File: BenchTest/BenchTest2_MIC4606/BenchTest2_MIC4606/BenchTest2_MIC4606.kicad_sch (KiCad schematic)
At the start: 46 parts, among them J1 Conn_01x01_Socket, J2 Conn_01x01_Socket, J3 Conn_01x01_Socket, J4 Conn_01x01_Socket, J5 Conn_01x01_Socket, J6 Conn_01x01_Socket, J9 Conn_01x02_Socket, Q1 Q_NMOS_GDS, Q2 Q_NMOS_GDS, Q3 Q_NMOS_GDS, Q4 Q_NMOS_GDS

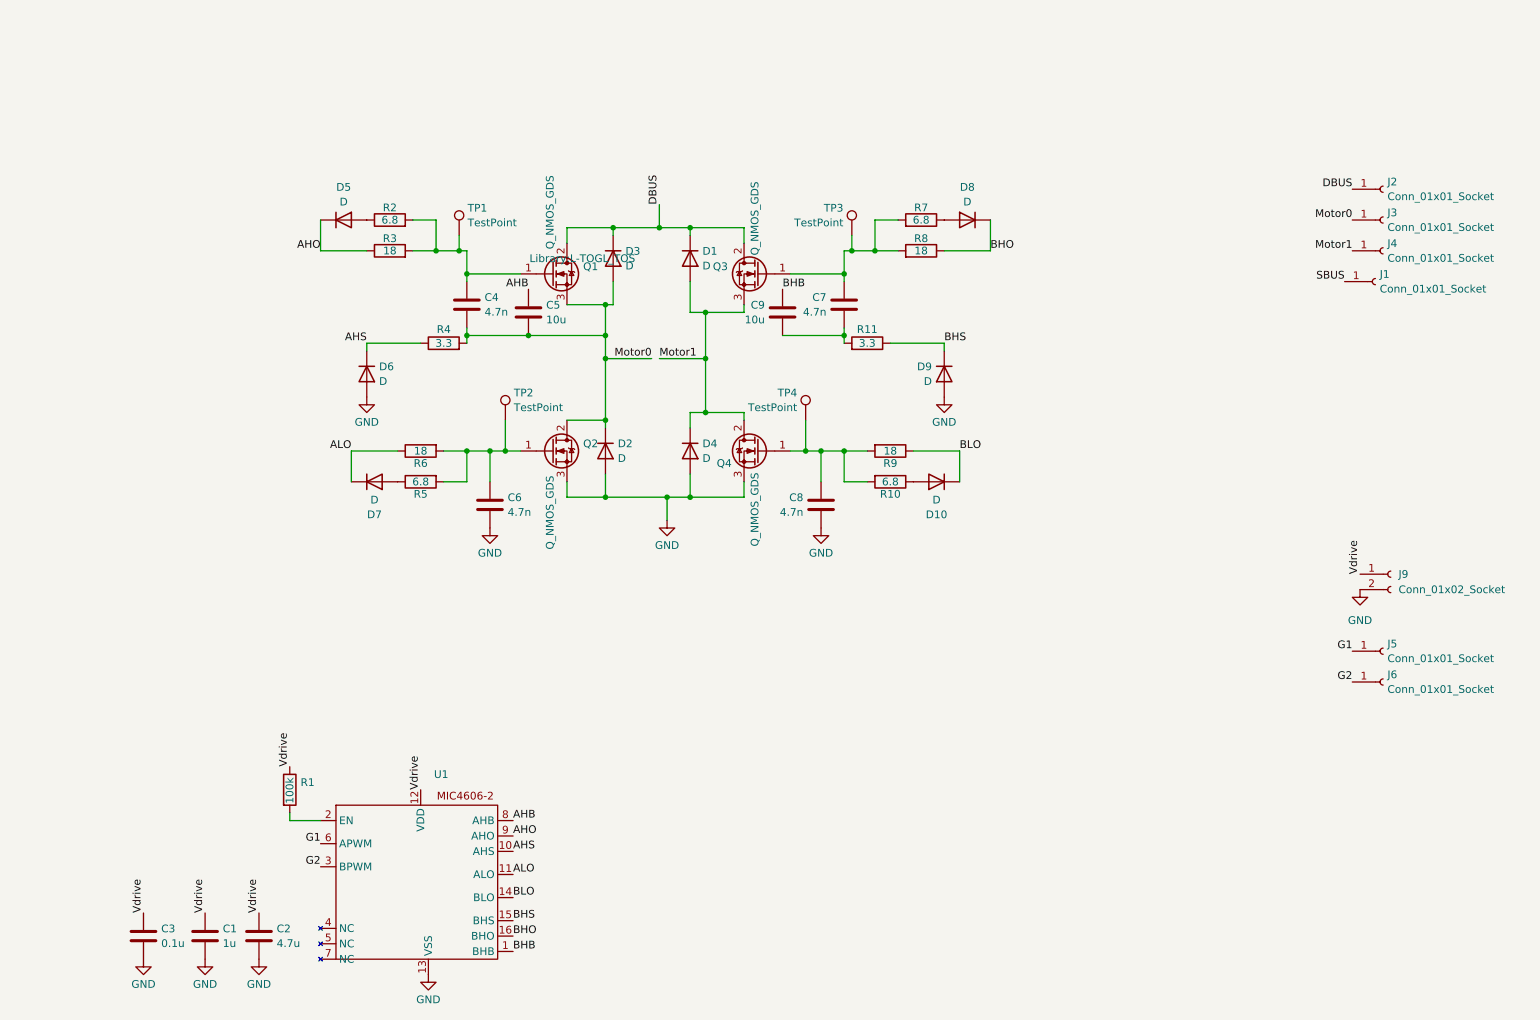
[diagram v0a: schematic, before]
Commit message: WIP - Creating Seperate board for controlling fet board
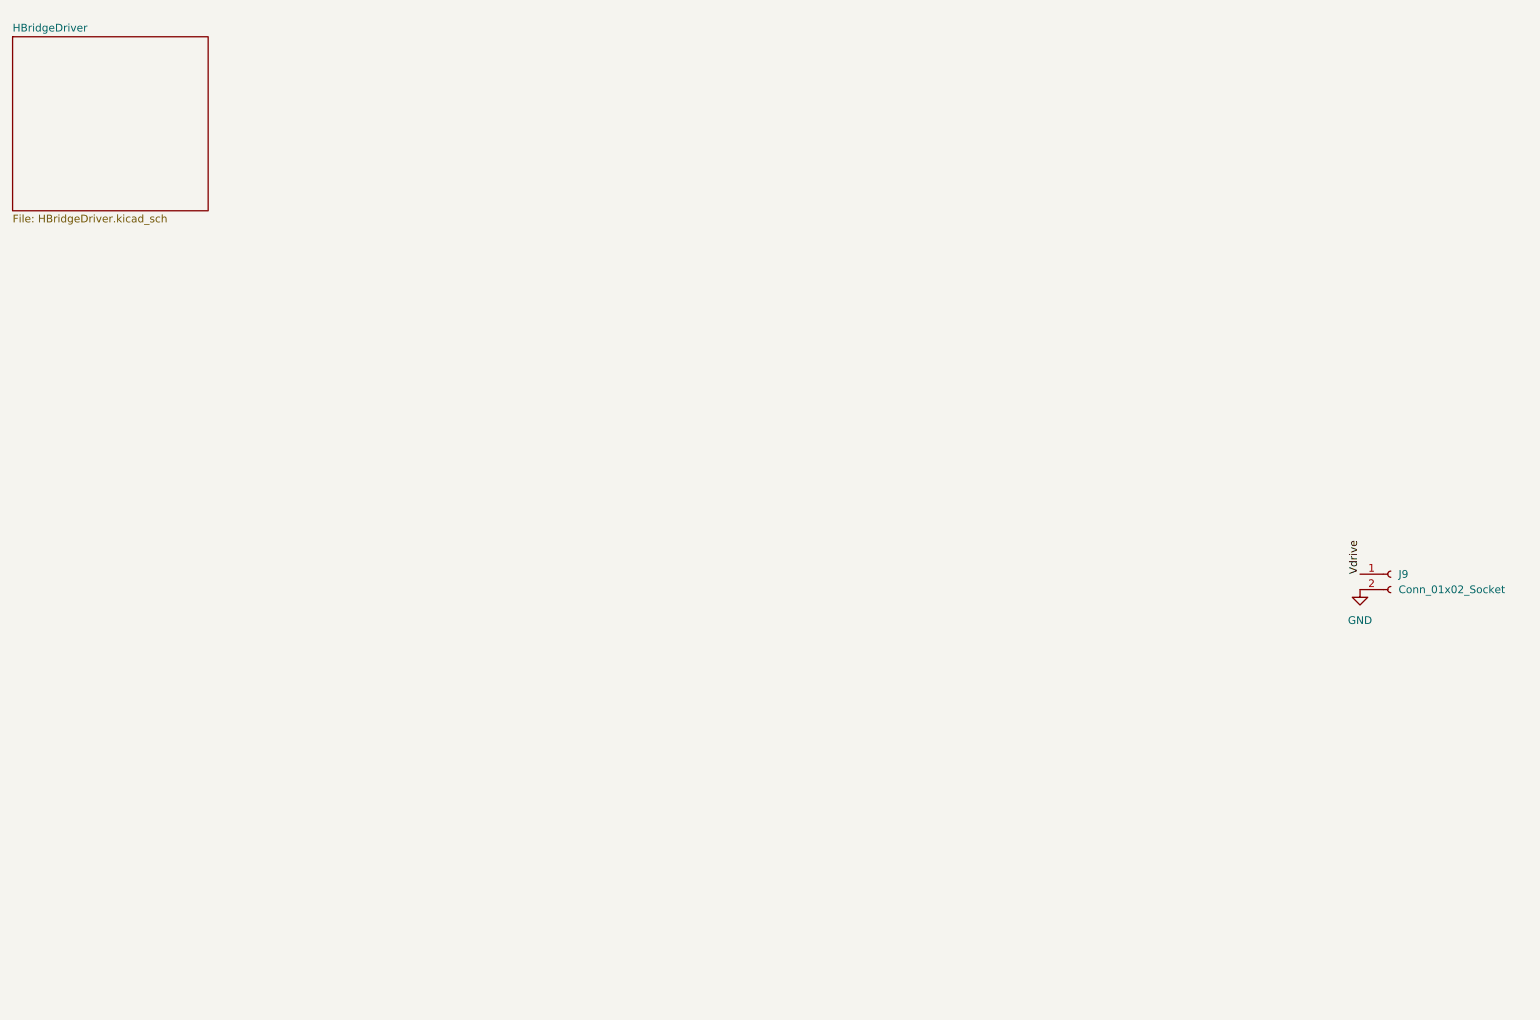
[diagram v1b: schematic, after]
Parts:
- removed C1: 1u, Capacitor_SMD:C_0603_1608Metric_Pad1.08x0.95mm_HandSolder, symbol Device:C
- removed C2: 4.7u, Capacitor_SMD:C_0603_1608Metric_Pad1.08x0.95mm_HandSolder, symbol Device:C
- removed C3: 0.1u, Capacitor_SMD:C_0603_1608Metric_Pad1.08x0.95mm_HandSolder, symbol Device:C
- removed C4, C6, C7, C8: 4.7n, Capacitor_SMD:C_0805_2012Metric_Pad1.18x1.45mm_HandSolder, symbol Device:C
- removed C5, C9: 10u, Capacitor_SMD:C_0805_2012Metric_Pad1.18x1.45mm_HandSolder, symbol Device:C
- removed D1, D10, D2, D3, D4, D5, D6, D7, D8, D9: D, Diode_SMD:D_SMB, symbol Device:D
- removed J1, J2, J3, J4: Conn_01x01_Socket, TerminalBlock_Wuerth:Wuerth_REDCUBE-THR_WP-THRSH_74651194_THR, symbol Connector:Conn_01x01_Socket
- removed J5, J6: Conn_01x01_Socket, Connector_PinHeader_2.54mm:PinHeader_1x01_P2.54mm_Vertical, symbol Connector:Conn_01x01_Socket
- removed Q1, Q2, Q3, Q4: Q_NMOS_GDS, Library:L-TOGL_TOS, symbol Device:Q_NMOS_GDS
- removed R1: 100k, Resistor_SMD:R_0402_1005Metric_Pad0.72x0.64mm_HandSolder, symbol Device:R
- removed R10, R2, R5, R7: 6.8, Resistor_SMD:R_0805_2012Metric_Pad1.20x1.40mm_HandSolder, symbol Device:R
- removed R11, R4: 3.3, Resistor_SMD:R_0805_2012Metric_Pad1.20x1.40mm_HandSolder, symbol Device:R
- removed R3, R6, R8, R9: 18, Resistor_SMD:R_0805_2012Metric_Pad1.20x1.40mm_HandSolder, symbol Device:R
- removed TP1, TP2, TP3, TP4: TestPoint, TestPoint:TestPoint_THTPad_1.0x1.0mm_Drill0.5mm, symbol Connector:TestPoint
- removed U1: ~, Package_SO:TSSOP-16_4.4x5mm_P0.65mm, symbol New_Library:MIC4606
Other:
- added sheet HBridgeDriver (HBridgeDriver.kicad_sch)

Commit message: Board to ship for Fets
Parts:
- added C10, C12: 0.1u, Capacitor_SMD:C_0402_1005Metric_Pad0.74x0.62mm_HandSolder, symbol Device:C
- added C11, C13: 2.2u, Capacitor_SMD:C_0603_1608Metric_Pad1.08x0.95mm_HandSolder, symbol Device:C
- added J10, J11, J12, J13, J14, J15: Conn_01x01_Socket, Connector_PinHeader_2.54mm:PinHeader_1x01_P2.54mm_Vertical, symbol Connector:Conn_01x01_Socket
- added R12, R13, R14: 33, Resistor_SMD:R_0402_1005Metric_Pad0.72x0.64mm_HandSolder, symbol Device:R
- added U2, U3: ~, Package_SO:SOIC-8_3.9x4.9mm_P1.27mm, symbol New_Library:FAN3217
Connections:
- net GND: now also C10.2, C11.2, C12.2, C13.2, U2.3 (GND), U3.3 (GND)
- net Vdrive: now also C10.1, C11.1, C12.1, C13.1, U2.6 (VDD), U3.6 (VDD)
- new net: R12.1, U2.5 (OUTB)
- new net: R14.1, U2.7 (OUTA)
- new net: R13.1, U3.7 (OUTA)
- new net G5: J10.1 (Pin_1), R14.2
- new net G6: J11.1 (Pin_1), R12.2
- new net G7: J12.1 (Pin_1), R13.2
- new net IN_G5: J13.1 (Pin_1), U2.2 (INA)
- new net IN_G6: J14.1 (Pin_1), U2.4 (INB)
- new net IN_G7: J15.1 (Pin_1), U3.2 (INA)
- no-connect marks 0 -> 2
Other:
- sheet HBridgeDriver ports: added Vdrive; removed none
